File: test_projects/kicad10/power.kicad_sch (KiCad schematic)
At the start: 21 parts, among them J3 Barrel_Jack_MountingPin, U3 LM3880, U4 AP2112K-1.8, U6 RT9742AGJ5F

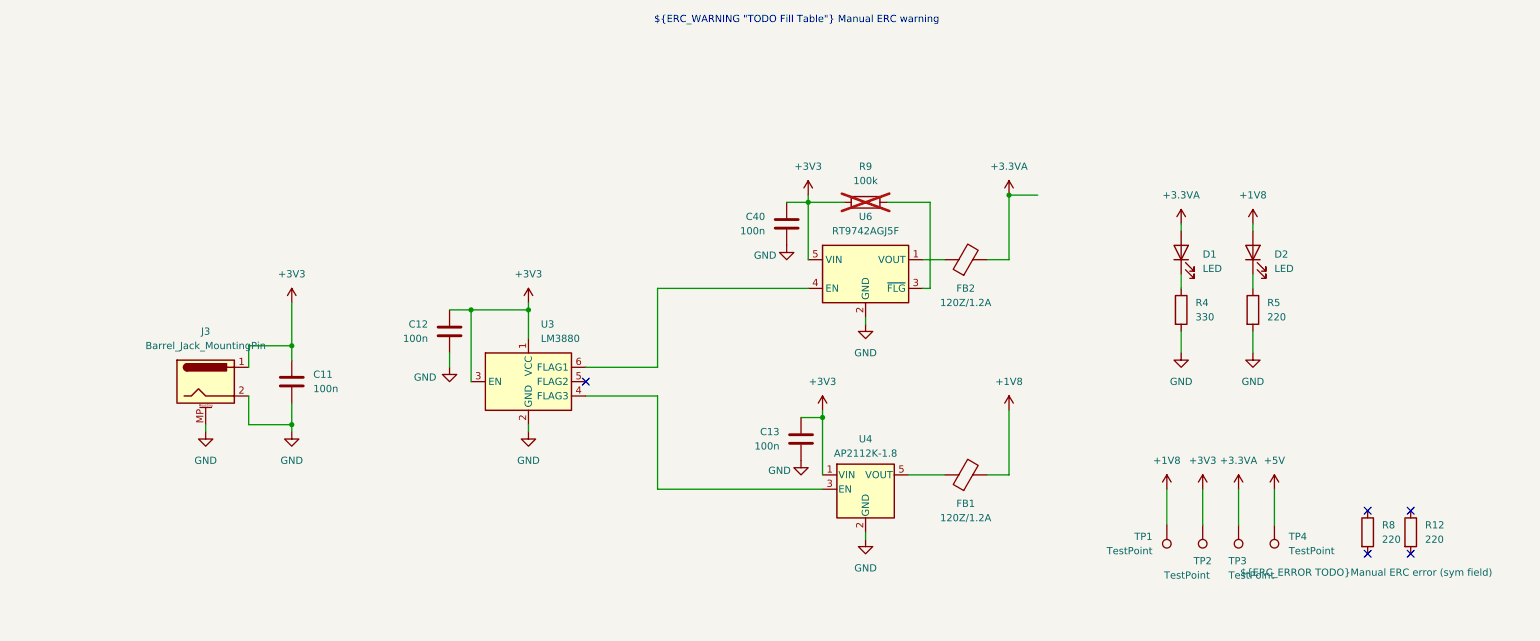
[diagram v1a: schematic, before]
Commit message: [#89355] test_projects: K10: Add additional features
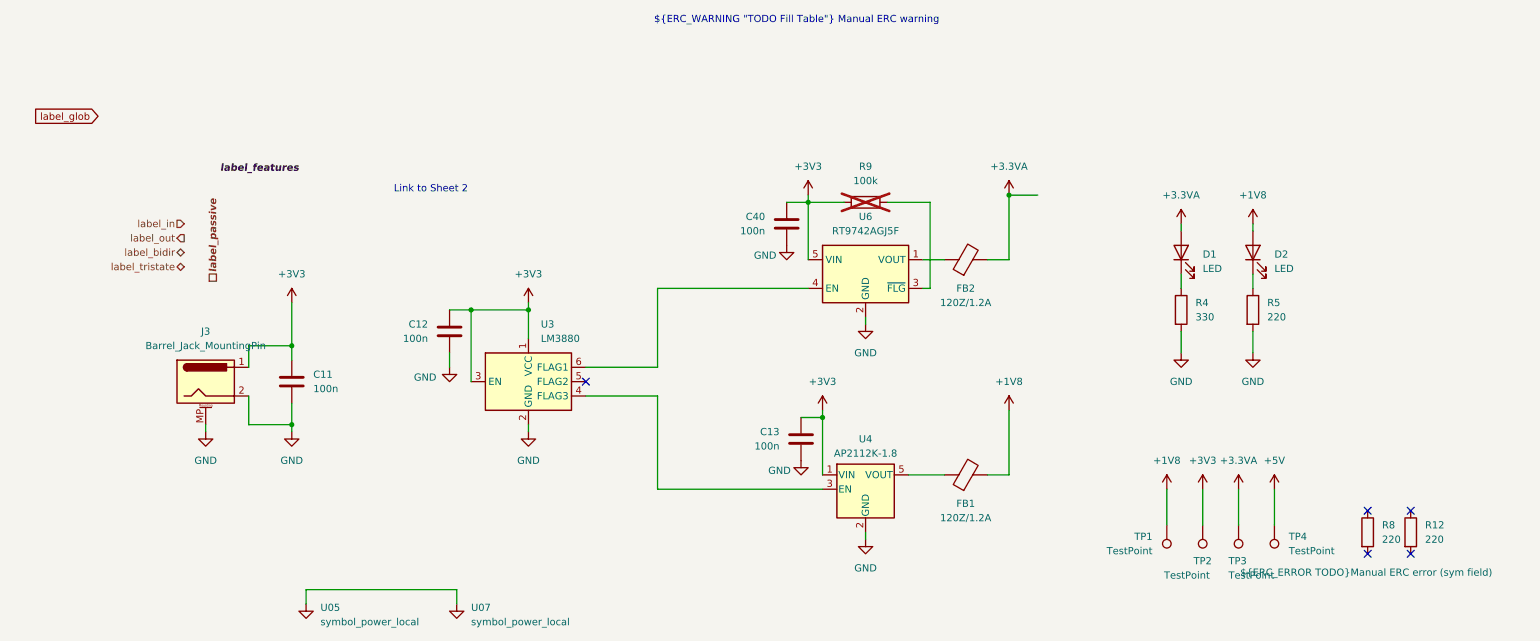
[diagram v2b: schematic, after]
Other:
- note added: "Link to Sheet 2"
